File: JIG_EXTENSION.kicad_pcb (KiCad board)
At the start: 2 copper layers, 180 x 180 mm, 114 parts, among them J1 Conn_01x03_Pin, J10 USB_B, J11 VIN, J12 Conn_01x02_Pin, J13 Conn_01x02_Pin, J14 Conn_01x02_Pin, J15 Conn_01x02_Pin, J16 Conn_01x02_Pin, J17 VIN, J18 Conn_01x04_Pin, J19 Conn_01x04_Pin, J20 Conn_01x04_Pin, J21 VIN, J22 Conn_02x04_Odd_Even, J3 Conn_01x07_Pin, J4 Conn_01x12_Socket, J5 Conn_01x12_Socket, J6 VIN, J7 618037231321, J8 Conn_01x18_Pin, J9 Conn_01x19_Pin, Q1 WST3325, U1 ESP32-DEVKIT-V1, U10 MCP2562-E-MF, U11 MAX13487EESAT, U2 CH340E, U3 AMS1117-3.3, U4 NCP1117DT50RKG, U5 SN74LVC1G3157DBVR, U6 SN74LVC1G3157DBVR, U9 MCP2515-xST, Y1 16MHz

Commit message: 1,1
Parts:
- added G***: LOGO, LOGO, F.Cu at (322.4, 80.4)
- added JP1: SolderJumper_2_Open, Jumper:SolderJumper-2_P1.3mm_Open_RoundedPad1.0x1.5mm, B.Cu at (270.8, 49.5)
- added JP2: SolderJumper_2_Open, Jumper:SolderJumper-2_P1.3mm_Open_RoundedPad1.0x1.5mm, B.Cu at (269.0, 29.3)
- added Q2: MMBT3904, Package_TO_SOT_SMD:SOT-23, F.Cu at (276.1, 36.8)
- added Q3: MMBT3904, Package_TO_SOT_SMD:SOT-23, F.Cu at (271.2, 41.3)
- added R58: 10k, Resistor_SMD:R_0603_1608Metric, F.Cu at (280.1, 37.8)
- added R59: 10k, Resistor_SMD:R_0603_1608Metric, F.Cu at (274.8, 40.3)
- added R60: 1K, Resistor_SMD:R_0603_1608Metric, F.Cu at (280.1, 34.9)
- added R61: 1K, Resistor_SMD:R_0603_1608Metric, F.Cu at (274.8, 42.0)
- D10, D11: footprint LED_SMD:LED_0805_2012Metric -> LED_SMD:LED_0603_1608Metric
- J1: footprint Connector_JST:JST_XH_S3B-XH-A_1x03_P2.50mm_Horizontal -> Connector_PinSocket_2.54mm:PinSocket_1x03_P2.54mm_Horizontal
- R53, R54: value 1K -> 2K
- moved D8 5.73 mm to (290.0, 43.5)
- moved R45 5.73 mm to (289.7, 39.3)
- moved D10 5.59 mm to (271.1, 31.6)
- moved R53 4.58 mm to (267.7, 31.6)
- moved D11 2.47 mm to (271.0, 34.3)
- moved R54 1.82 mm to (267.6, 34.2)
- moved R34 1.70 mm to (270.3, 46.0), turned to 90 degrees
- moved J1 0.58 mm to (287.6, 69.0), turned to 180 degrees
- moved R33 0.27 mm to (267.1, 44.5)
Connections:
- C13 pad 1: 3V3 -> 5V0
- C14 pad 1: 3V3 -> 5V0
- D10 pad 2: 3V3 -> 5V0
- D11 pad 2: 3V3 -> 5V0
- R32 pad 1: /UART_RS485_TX -> /UART_RS485_TX_5V
- R32 pad 2: 3V3 -> 5V0
- R33 pad 2: 3V3 -> 5V0
- R34 pad 1: /UART_RS485_RX -> /UART_RS485_RX_5V
- R34 pad 2: 3V3 -> 5V0
- R35 pad 2: 3V3 -> 5V0
- R40 pad 2: 3V3 -> 5V0
- R41 pad 2: 3V3 -> 5V0
- R53 pad 2: /UART_RS485_TX -> /UART_RS485_RX_5V
- R54 pad 2: /UART_RS485_RX -> /UART_RS485_TX_5V
- U11 pad 1: /UART_RS485_TX -> /UART_RS485_TX_5V
- U11 pad 4: /UART_RS485_RX -> /UART_RS485_RX_5V
- U11 pad 8: 3V3 -> 5V0
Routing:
- net 5V0: track 178.2 -> 246.1 mm
- net /UART_RS485_RX_5V: track 0.00 -> 45.7 mm, vias 0 -> 3
- net /UART_RS485_TX_5V: track 0.00 -> 33.9 mm, vias 0 -> 1
- net 3V3: track 263.8 -> 233.4 mm, vias 1 -> 3
- net /UART_RS485_RX: track 167.7 -> 189.8 mm, vias 4 -> 2
- net Net-(Q2-B): track 0.00 -> 4.51 mm
- net /UART_RS485_TX: track 161.8 -> 163.8 mm, vias 3 -> 4
- net Net-(Q3-B): track 0.00 -> 1.94 mm
- net Net-(U11-~{RE}): track 6.96 -> 8.61 mm, vias 0 -> 2
- net GND: track 60.6 -> 62.0 mm, vias 102 -> 108
- net Net-(D10-K): track 2.86 -> 1.77 mm
- net Net-(D11-K): track 2.78 -> 1.85 mm
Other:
- board text added: "GND TXD RXD"
- board text added: "ROAM JIG V1.0"

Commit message: delete jlink selector
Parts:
- removed J20: Conn_01x04_Pin, Connector_PinHeader_2.54mm:PinHeader_1x04_P2.54mm_Horizontal
- removed R51: 0, Resistor_SMD:R_0603_1608Metric
- removed R52: 10K, Resistor_SMD:R_0603_1608Metric
- removed U5, U6: SN74LVC1G3157DBVR, Package_TO_SOT_SMD:SOT-23-6
- added R57: 0, Resistor_SMD:R_0603_1608Metric, F.Cu at (228.0, 165.9)
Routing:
- net 3V3_B: track 381.7 -> 277.9 mm
- net /SWCLK: track 51.9 -> 24.0 mm, vias 1 -> 0
- net /SWD_SEL: track 23.5 -> 0.00 mm
- net /SWDIO: track 45.2 -> 25.0 mm, vias 1 -> 0
- net /VCU_SWDIO: track 28.3 -> 8.47 mm, vias 1 -> 0
- net /VCU_SWCLK: track 25.4 -> 13.2 mm, vias 2 -> 1
- net /SWCLK_OUT: track 8.44 -> 0.00 mm
- net /SWDIO_OUT: track 8.41 -> 0.00 mm
- net Net-(U1-D34): track 117.7 -> 116.3 mm
- net GND: vias 108 -> 106
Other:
- board text removed: "SET D34 LOW TO SELECT NRF"
- board text removed: "SWD SELECTOR"

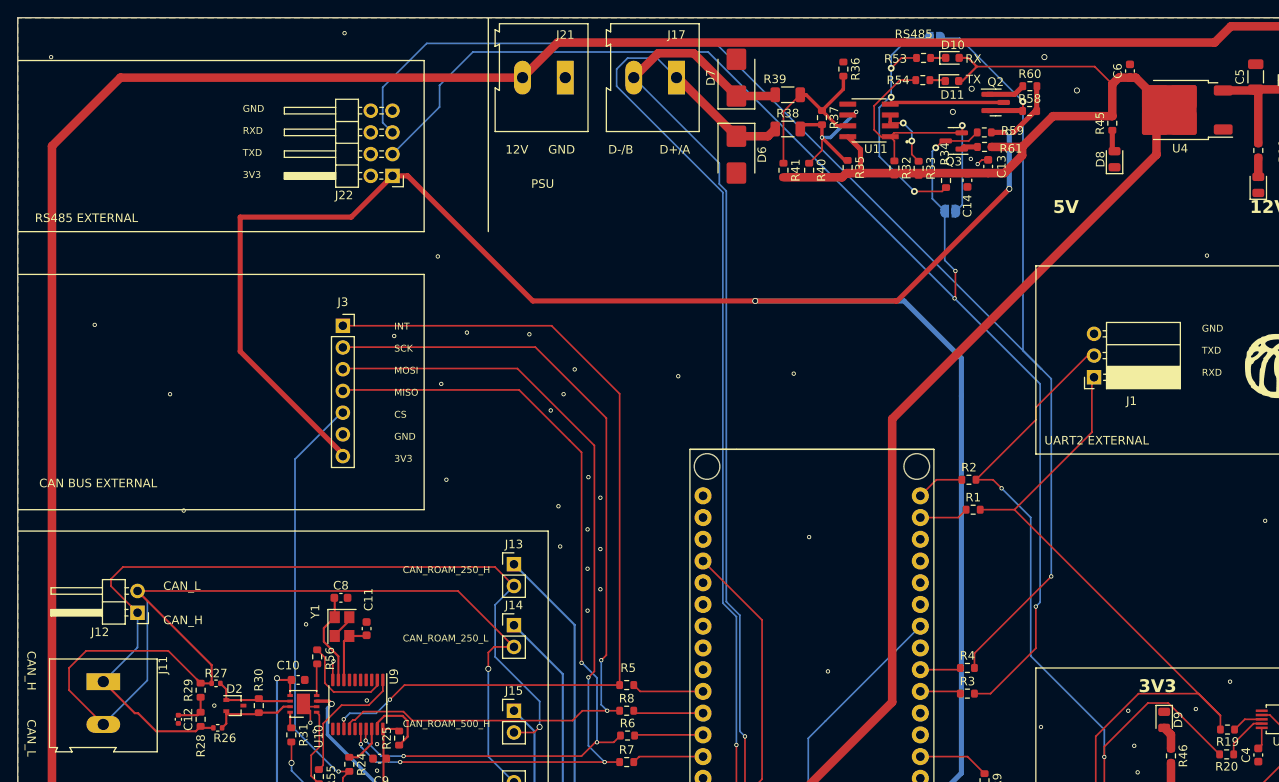
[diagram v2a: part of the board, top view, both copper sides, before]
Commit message: delete uart external rs485external
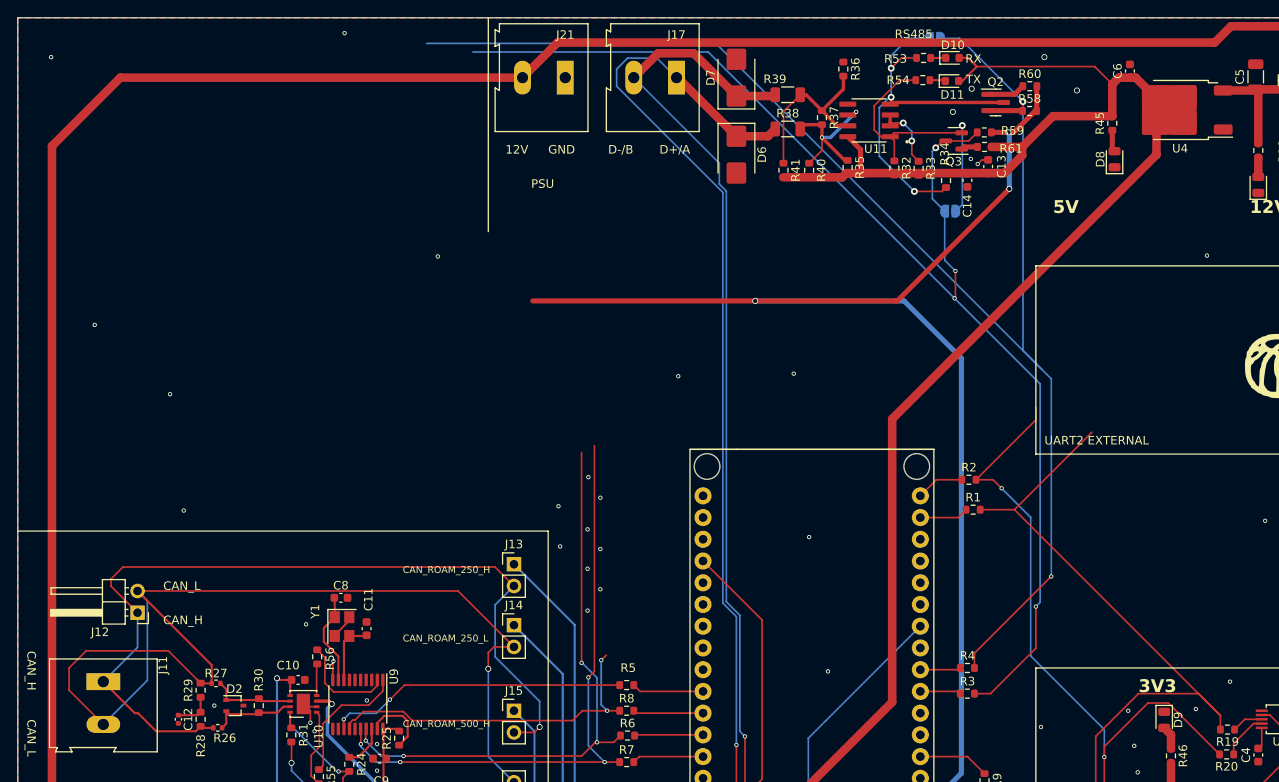
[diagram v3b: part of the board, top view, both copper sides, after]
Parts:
- removed J1: Conn_01x03_Pin, Connector_PinSocket_2.54mm:PinSocket_1x03_P2.54mm_Horizontal
- removed J22: Conn_02x04_Odd_Even, Connector_PinHeader_2.54mm:PinHeader_2x04_P2.54mm_Horizontal
- removed J3: Conn_01x07_Pin, Connector_PinSocket_2.54mm:PinSocket_1x07_P2.54mm_Vertical
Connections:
- U1 pad 19: Net-(U1-D34) -> unconnected-(U1-D34-Pad19)
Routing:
- net unconnected-(U1-D34-Pad19): track 0.00 -> 116.3 mm, vias 0 -> 2
- net Net-(U1-D34): track 116.3 -> 0.00 mm, vias 2 -> 0
- net 3V3: track 233.4 -> 158.5 mm
- net /CAN_INT: track 104.7 -> 35.0 mm
- net /SCK: track 102.7 -> 40.7 mm
- net /CS: track 134.2 -> 94.6 mm
- net /MOSI: track 104.3 -> 71.2 mm
- net /MISO: track 98.5 -> 67.6 mm
- net /UART_RS485_TX: track 163.8 -> 147.5 mm
- net /UART_RS485_RX: track 189.8 -> 176.8 mm
- net /UART_QT_TX: track 87.1 -> 77.8 mm
- net /UART_QT_RX: track 93.4 -> 86.5 mm
- net GND: vias 106 -> 98
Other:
- board text removed: "CAN BUS EXTERNAL"
- board text removed: "GND RXD TXD 3V3"
- board text removed: "GND TXD RXD"
- board text removed: "INT SCK MOSI MISO CS GND 3V3"
- board text removed: "RS485 EXTERNAL"
